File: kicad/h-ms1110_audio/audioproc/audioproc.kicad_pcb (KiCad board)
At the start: 2 copper layers, 99.1 x 99.1 mm, 16 parts, among them J1 EXT_INPUT, J2 SYNC, J3 ROT, J4 CONTROL, J5 H-MS1110_Bus, J6 FP_POWER, J7 AUDIO, J8 I2C, U1 LM7805_TO220, U2 L78L12_TO92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

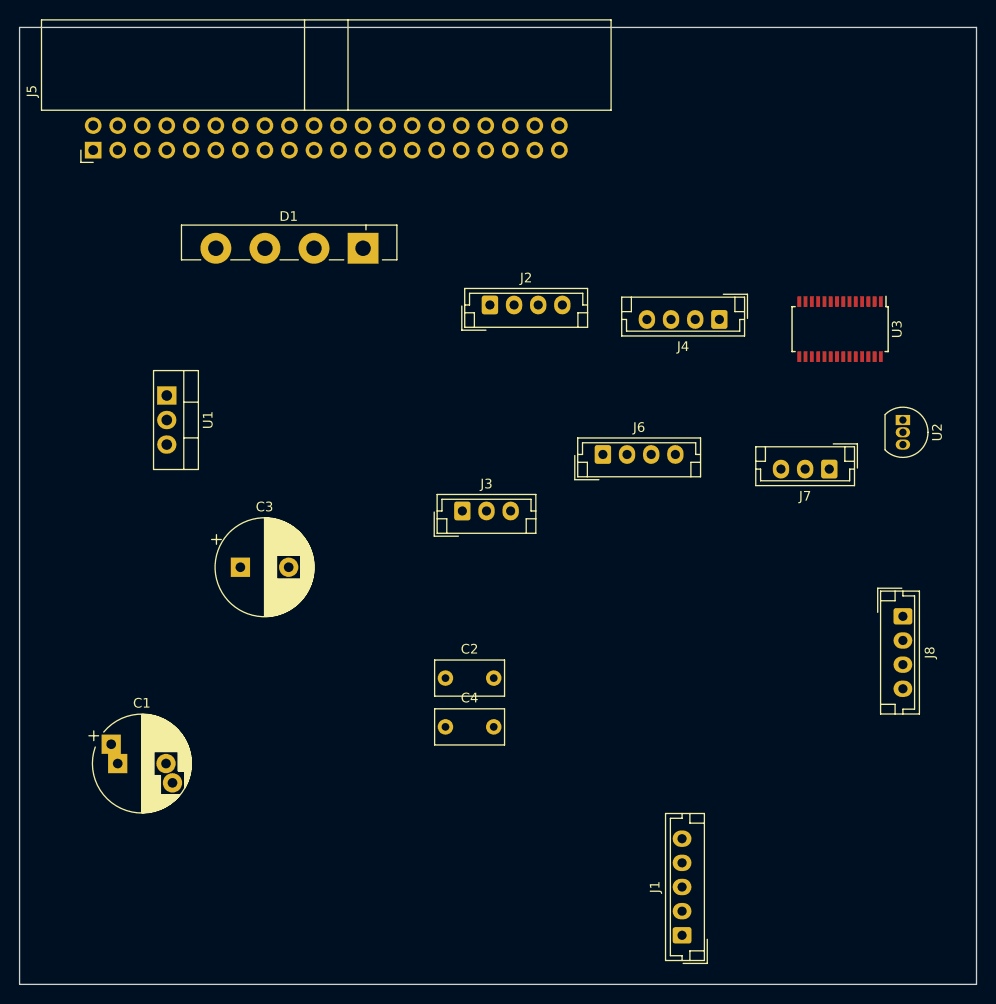
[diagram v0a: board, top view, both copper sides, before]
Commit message: Add MP1584 module symbols
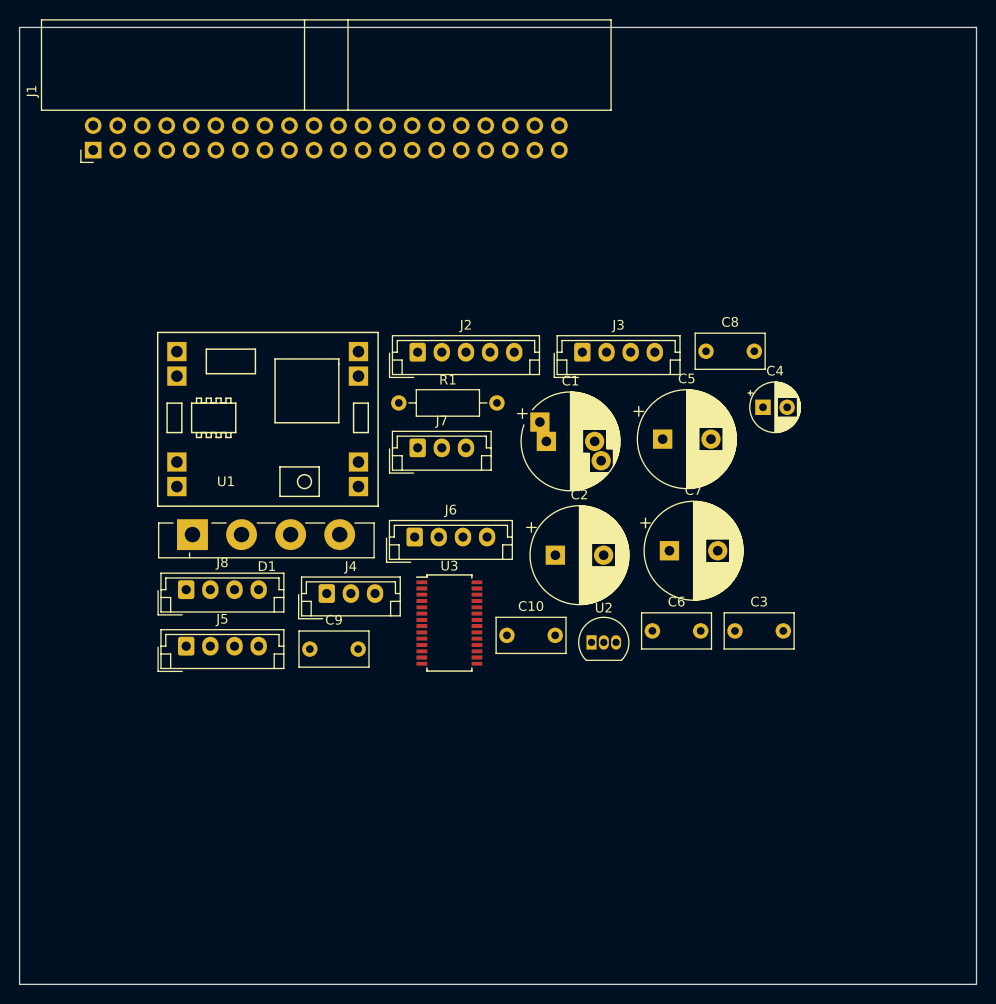
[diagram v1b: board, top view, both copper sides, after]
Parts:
- removed the J1 at (167.6, 127.0)
- added C10: 2.2, Capacitor_THT:C_Rect_L7.0mm_W3.5mm_P5.00mm, F.Cu at (149.5, 96.0)
- added C5: 220.0, Capacitor_THT:CP_Radial_D10.0mm_P5.00mm, F.Cu at (165.6, 75.6)
- added C6: 0.1, Capacitor_THT:C_Rect_L7.0mm_W3.5mm_P5.00mm, F.Cu at (164.6, 95.5)
- added C7: 220.0, Capacitor_THT:CP_Radial_D10.0mm_P5.00mm, F.Cu at (166.3, 87.2)
- added C8: 0.1, Capacitor_THT:C_Rect_L7.0mm_W3.5mm_P5.00mm, F.Cu at (170.1, 66.5)
- added C9: 2.2, Capacitor_THT:C_Rect_L7.0mm_W3.5mm_P5.00mm, F.Cu at (129.1, 97.4)
- added J5: CONTROL, Connector_JST:JST_EH_B4B-EH-A_1x04_P2.50mm_Vertical, F.Cu at (116.3, 97.1)
- added R1: 100, Resistor_THT:R_Axial_DIN0207_L6.3mm_D2.5mm_P10.16mm_Horizontal, F.Cu at (138.3, 71.9)
- C1: value 4700.0 -> 1000.0
- C2: value 0.1 -> 470.0; footprint Capacitor_THT:C_Rect_L7.0mm_W3.5mm_P5.00mm -> Capacitor_THT:CP_Radial_D10.0mm_P5.00mm
- C3: value 1000.0 -> 0.1; footprint Capacitor_THT:CP_Radial_D10.0mm_P5.00mm -> Capacitor_THT:C_Rect_L7.0mm_W3.5mm_P5.00mm
- C4: value 0.1 -> 10.0; footprint Capacitor_THT:C_Rect_L7.0mm_W3.5mm_P5.00mm -> Capacitor_THT:CP_Radial_D5.0mm_P2.50mm
- J2: value SYNC -> EXT_INPUT; footprint Connector_JST:JST_EH_B4B-EH-A_1x04_P2.50mm_Vertical -> Connector_JST:JST_EH_B5B-EH-A_1x05_P2.50mm_Vertical
- J3: value ROT -> SYNC; footprint Connector_JST:JST_EH_B3B-EH-A_1x03_P2.50mm_Vertical -> Connector_JST:JST_EH_B4B-EH-A_1x04_P2.50mm_Vertical
- J4: value CONTROL -> ROT; footprint Connector_JST:JST_EH_B4B-EH-A_1x04_P2.50mm_Vertical -> Connector_JST:JST_EH_B3B-EH-A_1x03_P2.50mm_Vertical
- J7: value AUDIO -> SPECT
- U1: value LM7805_TO220 -> MP1584EN_module; footprint Package_TO_SOT_THT:TO-220-3_Vertical -> h-ms1110:MP1584EN_module
- moved J8 74.2 mm to (116.3, 91.2), turned to 0 degrees
- moved C1 55.5 mm to (153.6, 75.9)
- moved C3 51.6 mm to (173.1, 95.5)
- moved U3 50.6 mm to (143.6, 94.7), turned to 0 degrees
- moved J4 49.6 mm to (130.9, 91.6), turned to 0 degrees
- moved C4 46.6 mm to (176.0, 72.3)
- moved J7 42.7 mm to (140.3, 76.5), turned to 0 degrees
- moved U2 39.6 mm to (158.3, 96.7), turned to 0 degrees
- moved D1 34.5 mm to (117.0, 85.5), turned to 0 degrees
- moved J6 21.3 mm to (140.0, 85.8)
- moved J3 20.6 mm to (157.3, 66.6)
- moved C2 17.1 mm to (154.5, 87.7)
- moved U1 10.9 mm to (125.0, 73.4), turned to 0 degrees
- moved J2 8.94 mm to (140.3, 66.6)
- renumbered J5 to J1
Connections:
- net /TUN-L renamed /TUN_L
- net /TUN-R renamed /TUN_R
- net Net-(U3-Pad10) renamed /AUX1_L
- net Net-(U3-Pad11) renamed /AUX1_R
- net Net-(U3-Pad12) renamed /AUX2_L
- net Net-(U3-Pad13) renamed /AUX2_R
- net Net-(U3-Pad3) renamed /DIG_L
- net Net-(U3-Pad4) renamed /DIG_R
- C2 pad 1: Net-(C1-Pad1) -> +5V
- C4 pad 1: +5V -> Net-(C4-Pad1)
- C4 pad 2: GNDD -> GNDA
- J1 pad 23: Net-(J5-Pad23) -> /QD_G
- J1 pad 26: Net-(J5-Pad26) -> /QD_L
- J1 pad 28: Net-(J5-Pad28) -> /QD_R
- J1 pad 32: Net-(J5-Pad32) -> Net-(J1-Pad32)
- J1 pad 36: /MP3-L -> /MP3_L
- J1 pad 37: /MP3-R -> /MP3_R
- J2 pad 1: Net-(J2-Pad1) -> /+3.3VA
- J2 pad 2: /SYNC_DATA -> /AD2
- J2 pad 3: /SYNC_SCK -> /AD1
- J2 pad 4: GNDD -> /AD3
- J3 pad 1: /ROT-B -> Net-(J3-Pad1)
- J3 pad 2: GNDD -> /SYNC_DATA
- J3 pad 3: /ROT-A -> /SYNC_SCK
- J4 pad 1: /MUTE -> /ROT-B
- J4 pad 2: /STBY -> GNDD
- J4 pad 3: /REMOTE -> /ROT-A
- U1 pad 2: GNDD -> Net-(C1-Pad1)
- U1 pad 3: +5V -> GNDD
- U2 pad 3: Net-(J5-Pad32) -> Net-(C5-Pad1)
- U3 pad 14: Net-(U3-Pad14) -> Net-(C4-Pad1)
- U3 pad 18: /OUT_R -> Net-(C10-Pad1)
- U3 pad 21: /OUT_L -> Net-(C9-Pad1)
- U3 pad 5: Net-(U3-Pad5) -> /MP3_L
- U3 pad 6: Net-(U3-Pad6) -> /MP3_R
- U3 pad 7: Net-(U3-Pad7) -> /QD_L
- U3 pad 8: Net-(U3-Pad8) -> /QD_G
- U3 pad 9: Net-(U3-Pad9) -> /QD_R
